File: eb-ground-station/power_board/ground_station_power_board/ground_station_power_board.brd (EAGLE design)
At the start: 135 x 78 mm, 83 parts, among them J1 CONN_20X2SHROUDED, Q1 SQJ459EP_MOSFET_P_CHAN, Q15 DMN61D8LVT-DUAL-N-CHANNEL-MOS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, Q17 DMN61D8LVT-DUAL-N-CHANNEL-MOS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, Q18 DMN61D8LVT-DUAL-N-CHANNEL-MOS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, Q2 SQJ459EP_MOSFET_P_CHAN, Q22 TC4427-FET-GATE-DRVR, Q23 TC4427-FET-GATE-DRVR, Q24 TC4427-FET-GATE-DRVR, Q3 SQJ459EP_MOSFET_P_CHAN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

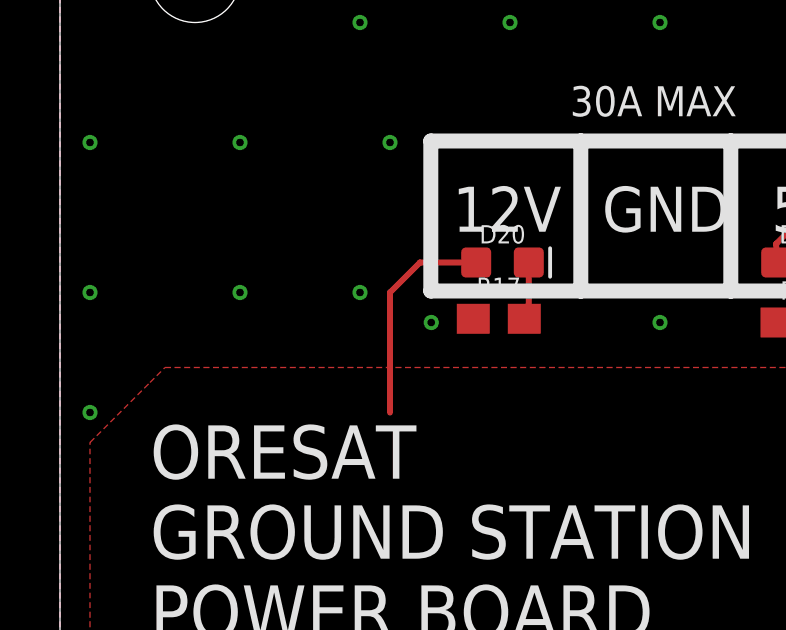
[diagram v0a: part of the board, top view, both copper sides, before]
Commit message: fixed logo
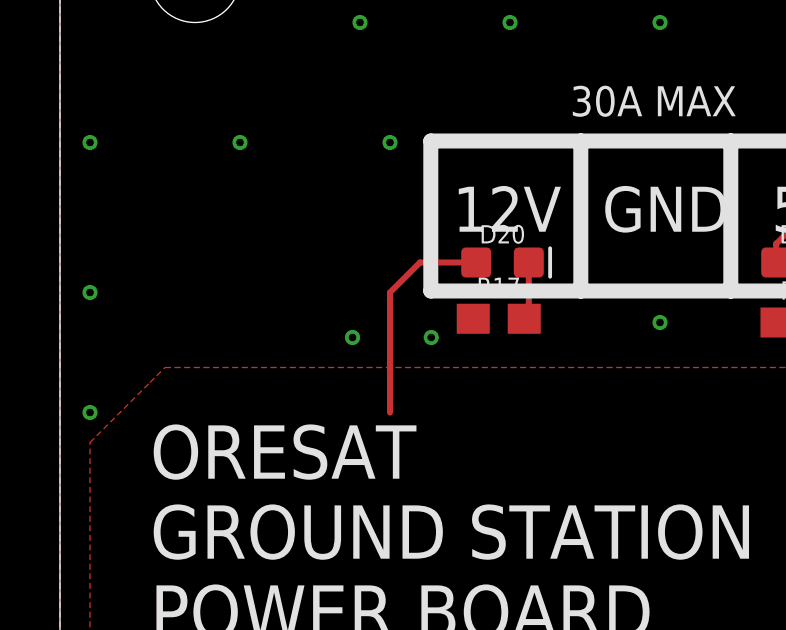
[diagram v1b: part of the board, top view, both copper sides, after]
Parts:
- moved U$8 9.40 mm to (25.0, 51.2)
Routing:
- net GND: vias 477 -> 476
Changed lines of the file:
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@@
 <layer number="27" name="tValues" color="7" fill="1" visible="no" active="yes"/>
 <layer number="28" name="bValues" color="7" fill="1" visible="no" active="yes"/>
-<layer number="29" name="tStop" color="7" fill="3" visible="no" active="yes"/>
-<layer number="30" name="bStop" color="7" fill="6" visible="no" active="yes"/>
+<layer number="29" name="tStop" color="7" fill="3" visible="yes" active="yes"/>
+<layer number="30" name="bStop" color="7" fill="6" visible="yes" active="yes"/>
 <layer number="31" name="tCream" color="7" fill="4" visible="no" active="yes"/>
 <layer number="32" name="bCream" color="7" fill="5" visible="no" active="yes"/>
@@
 <attribute name="VALUE" x="110.23" y="55.984" size="0.6096" layer="27" font="vector" ratio="20" align="top-left"/>
 </element>
-<element name="U$8" library="Oliver_Custom" package="PSAS_LOGO_15X15" value="" x="20.5" y="43" rot="MR0"/>
+<element name="U$8" library="Oliver_Custom" package="PSAS_LOGO_15X15" value="" x="25" y="51.25" rot="MR0"/>
 <element name="C11" library="SparkFun-Capacitors" package="0603" value="0.1uF" x="122.375" y="6">
 <attribute name="PROD_ID" value="CAP-08604" x="122.375" y="6" size="1.778" layer="27" display="off"/>
@@
 <via x="20" y="46" extent="1-16" drill="0.254"/>
 <via x="20" y="44" extent="1-16" drill="0.254"/>
-<via x="12.375" y="62" extent="1-16" drill="0.254"/>
+<via x="12.375" y="61.5" extent="1-16" drill="0.254"/>
 <via x="77.625" y="52.5" extent="1-16" drill="0.254"/>
 <via x="76" y="50.25" extent="1-16" drill="0.254"/>
@@
 <via x="1" y="63" extent="1-16" drill="0.254"/>
 <via x="1" y="59" extent="1-16" drill="0.254"/>
-<via x="6" y="63" extent="1-16" drill="0.254"/>
 <via x="6" y="68" extent="1-16" drill="0.254"/>
 <via x="11" y="68" extent="1-16" drill="0.254"/>
-<via x="10" y="63" extent="1-16" drill="0.254"/>
 <via x="10" y="72" extent="1-16" drill="0.254"/>
 <via x="15" y="72" extent="1-16" drill="0.254"/>
@@
 <via x="124" y="52" extent="1-16" drill="0.254"/>
 <via x="124" y="45" extent="1-16" drill="0.254"/>
+<via x="9.75" y="61.5" extent="1-16" drill="0.254"/>
 </signal>
 <signal name="OUT16">
